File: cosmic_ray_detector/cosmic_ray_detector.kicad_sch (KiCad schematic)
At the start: 10 parts, among them J2 5 pin pin header, J3 Black Banana, J4 Red Banana, J5 Green Banana, J6 BNC

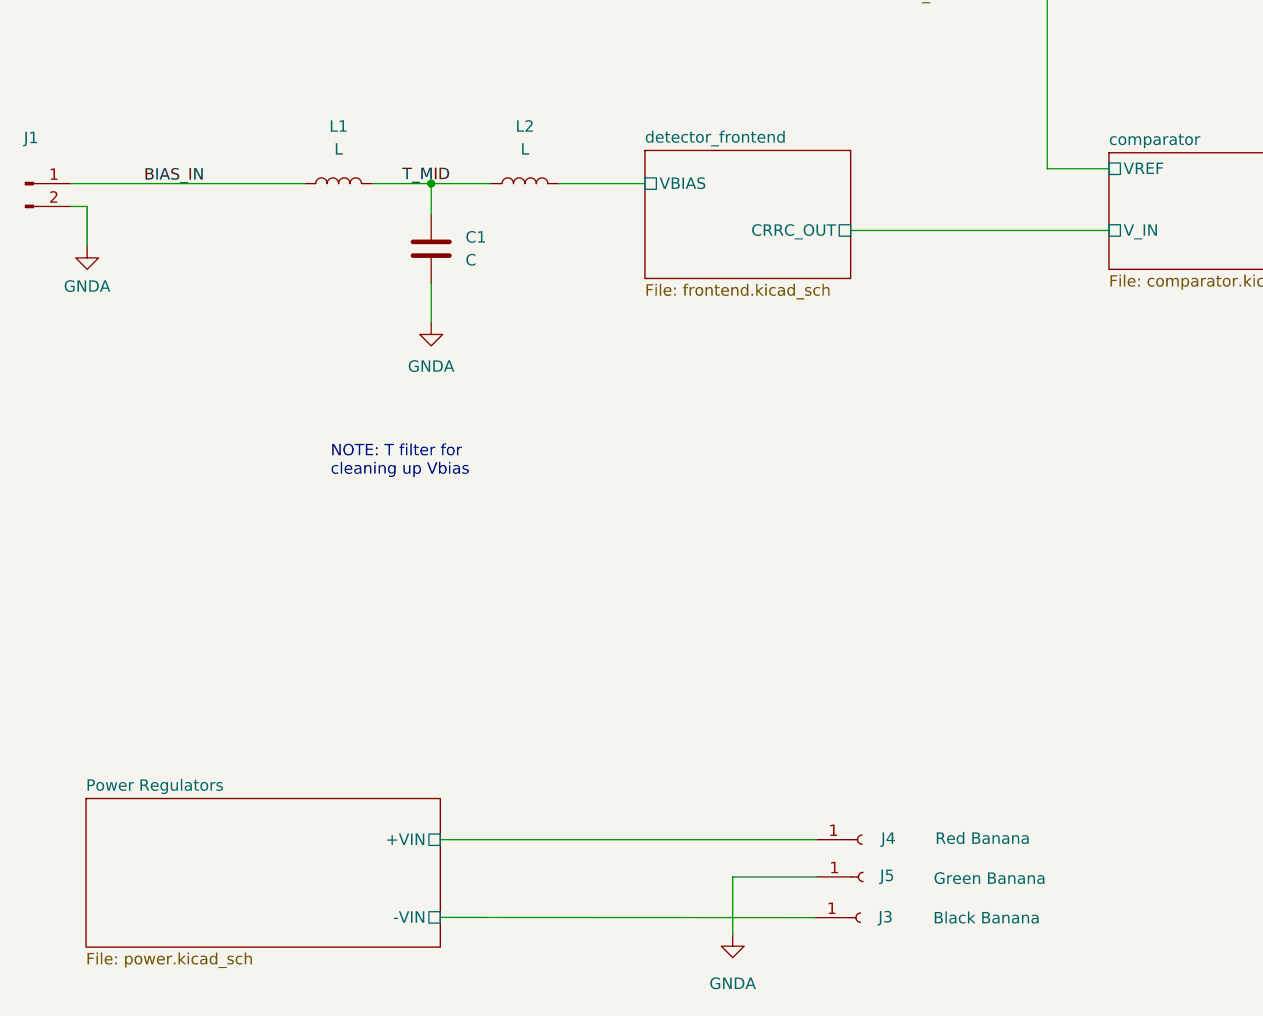
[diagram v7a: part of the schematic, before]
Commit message: updated, now passes ERC
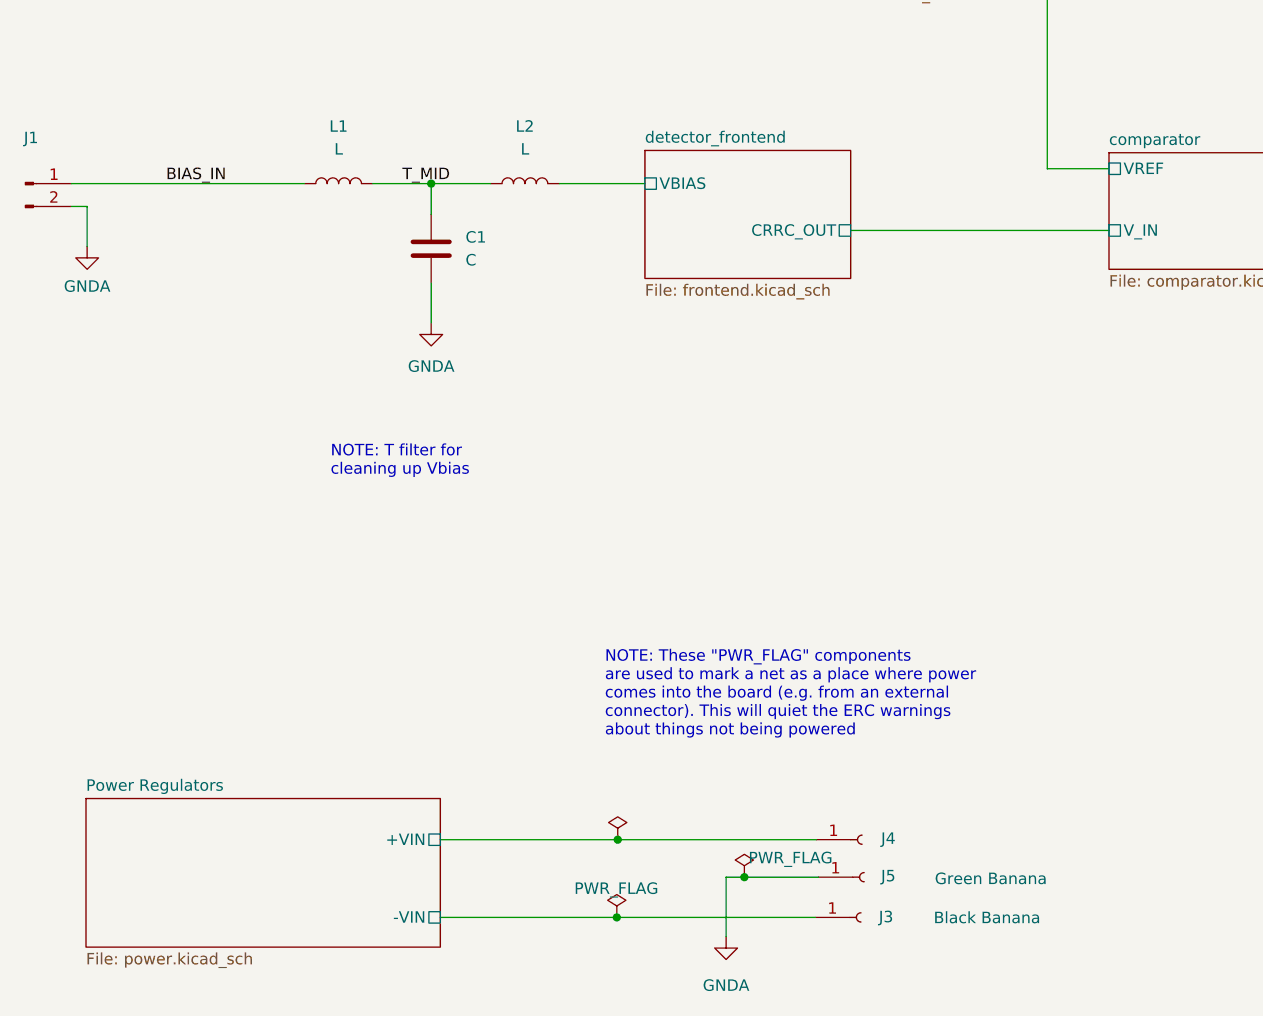
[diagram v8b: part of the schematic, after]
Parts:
- J4: value Red Banana -> (none)
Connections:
- net BIAS_IN: now also J1.1 (Pin_1), L1.1
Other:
- note added: "NOTE: These "PWR_FLAG" components are used to mark a net as a place where power comes into the board (e.g. from an external connector). This will quiet the ERC warnings about things not being powered"
